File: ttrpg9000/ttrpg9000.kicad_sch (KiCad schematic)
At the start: 31 parts, among them SW1 SW_SPST, SW2 RotaryEncoder, SW3 RotaryEncoder, SW4 SW_Push, U1 LP2950-3.3_TO92, U2 ATtiny2313A-P

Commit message: Second pass of schematic, start layout
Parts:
- removed C1: 47u, symbol Device:C
- removed C14, C15, C9: 0.01u, symbol Device:C
- removed R7, R8: 10k, symbol Device:R
- removed SW2, SW3: RotaryEncoder, symbol Device:RotaryEncoder
- removed SW4: SW_Push, symbol Switch:SW_Push
- added C1: 47u, Capacitor_THT:CP_Radial_D5.0mm_P2.00mm, symbol Device:C_Polarized
- added C16, C4, C5, C7: 0.01u, Capacitor_THT:C_Axial_L5.1mm_D3.1mm_P7.50mm_Horizontal, symbol Device:C
- added R1, R2, R4: 10k, Resistor_THT:R_Axial_DIN0204_L3.6mm_D1.6mm_P5.08mm_Vertical, symbol Device:R
- added R12: 1M, Resistor_THT:R_Axial_DIN0204_L3.6mm_D1.6mm_P5.08mm_Vertical, symbol Device:R
- added R3, R9: 20k, Resistor_THT:R_Axial_DIN0204_L3.6mm_D1.6mm_P5.08mm_Vertical, symbol Device:R
- added SW2, SW3: RotaryEncoder_Switch, Project:PEC12R-4xxxF-Nxxxx, symbol Device:RotaryEncoder_Switch
- BT1: footprint (none) -> Project:BAT_BH800S
- C10, C11, C12, C13, C2, C3, C6: footprint (none) -> Capacitor_THT:C_Axial_L5.1mm_D3.1mm_P7.50mm_Horizontal
- C14: renamed from C4; footprint (none) -> Capacitor_THT:C_Axial_L5.1mm_D3.1mm_P7.50mm_Horizontal
- C15: renamed from C5; footprint (none) -> Capacitor_THT:C_Axial_L5.1mm_D3.1mm_P7.50mm_Horizontal
- C8: renamed from C7; footprint (none) -> Capacitor_THT:C_Axial_L5.1mm_D3.1mm_P7.50mm_Horizontal
- C9: renamed from C8; footprint (none) -> Capacitor_THT:C_Axial_L5.1mm_D3.1mm_P7.50mm_Horizontal
- DS1: footprint (none) -> Project:DOGM204
- R10: renamed from R3; footprint (none) -> Resistor_THT:R_Axial_DIN0204_L3.6mm_D1.6mm_P5.08mm_Vertical
- R11: renamed from R4; footprint (none) -> Resistor_THT:R_Axial_DIN0204_L3.6mm_D1.6mm_P5.08mm_Vertical
- R5: footprint (none) -> Resistor_THT:R_Axial_DIN0204_L3.6mm_D1.6mm_P5.08mm_Vertical
- R6: value 10k -> 1M; footprint (none) -> Resistor_THT:R_Axial_DIN0204_L3.6mm_D1.6mm_P5.08mm_Vertical
- R7: renamed from R1; footprint (none) -> Resistor_THT:R_Axial_DIN0204_L3.6mm_D1.6mm_P5.08mm_Vertical
- R8: renamed from R2; footprint (none) -> Resistor_THT:R_Axial_DIN0204_L3.6mm_D1.6mm_P5.08mm_Vertical
- SW1: footprint (none) -> Project:SW3x1_L101011ML04Q_CNK
- renumbered U2 to U1, U1 to U2
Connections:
- net +3V3: now also R10.1, R8.2, R2.2, R4.1, SW2.S2, SW3.S2
- net +6V: now also C1.1; no longer R10.1, R6.2, R8.2
- net GND: now also C15.1, R6.2, C1.2, C16.2, C4.2, C5.1, C7.2, R12.2, SW2.C, SW3.C; no longer C15.2
- net at R5.1: now also C5.2, R4.2, SW2.A; no longer U1.6 (PD2)
- net at R5.2: now also U1.8 (PD4); no longer R6.1
- net at C14.1, R7.2, R8.1: now also SW3.B
- net at R10.2, R11.1: now also C15.2, SW3.A; no longer C15.1
- net at R7.1: now also U1.6 (PD2); no longer U1.8 (PD4)
- net at U1.2 (PD0): now also C16.1, R12.1, R9.2
- net at U1.3 (PD1): now also R11.2
- net at U1.7 (PD3): now also R6.1, C7.1, R3.2; no longer R11.2
- net at U1.9 (PD5): now also R1.1
- new net: R9.1, SW3.S1
- new net: C4.1, R1.2, R2.1, SW2.B
- new net: R3.1, SW2.S1
- no-connect marks 5 -> 4
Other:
- moved on the sheet: C10, C11, C12, C13, C14, C15, C6, C8, C9, DS1, R10, R11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

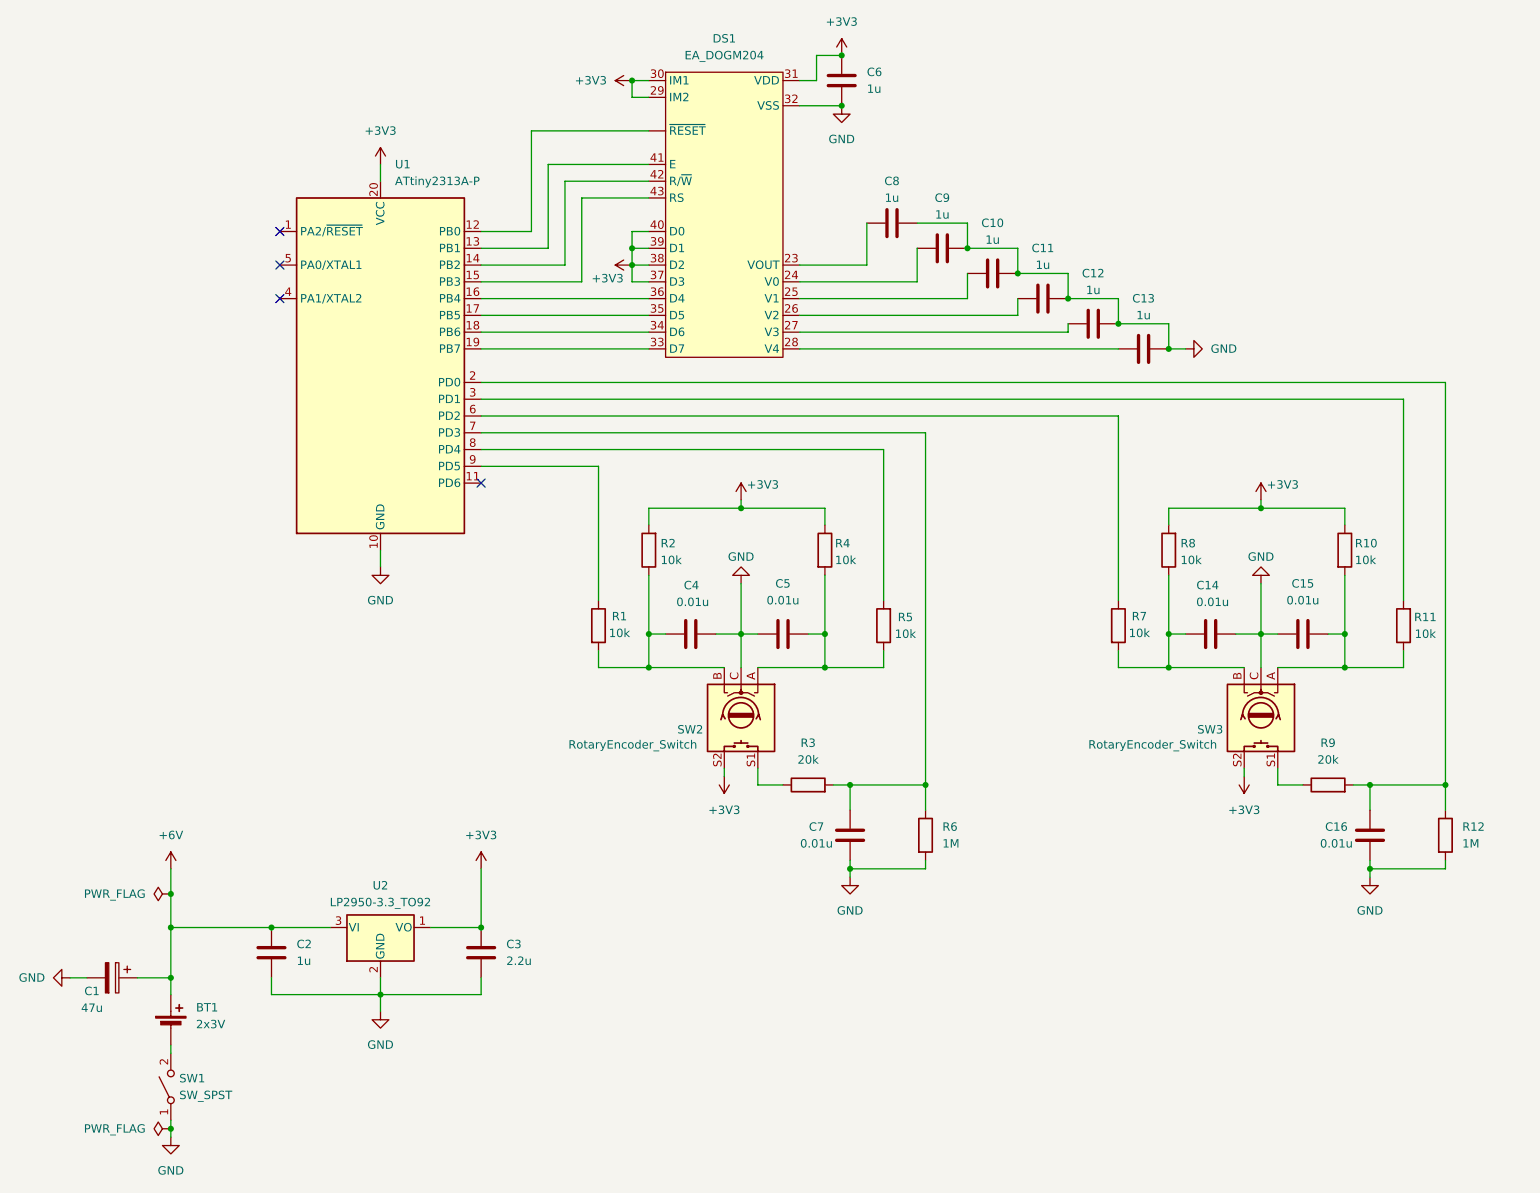
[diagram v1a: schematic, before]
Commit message: Clean up board layout
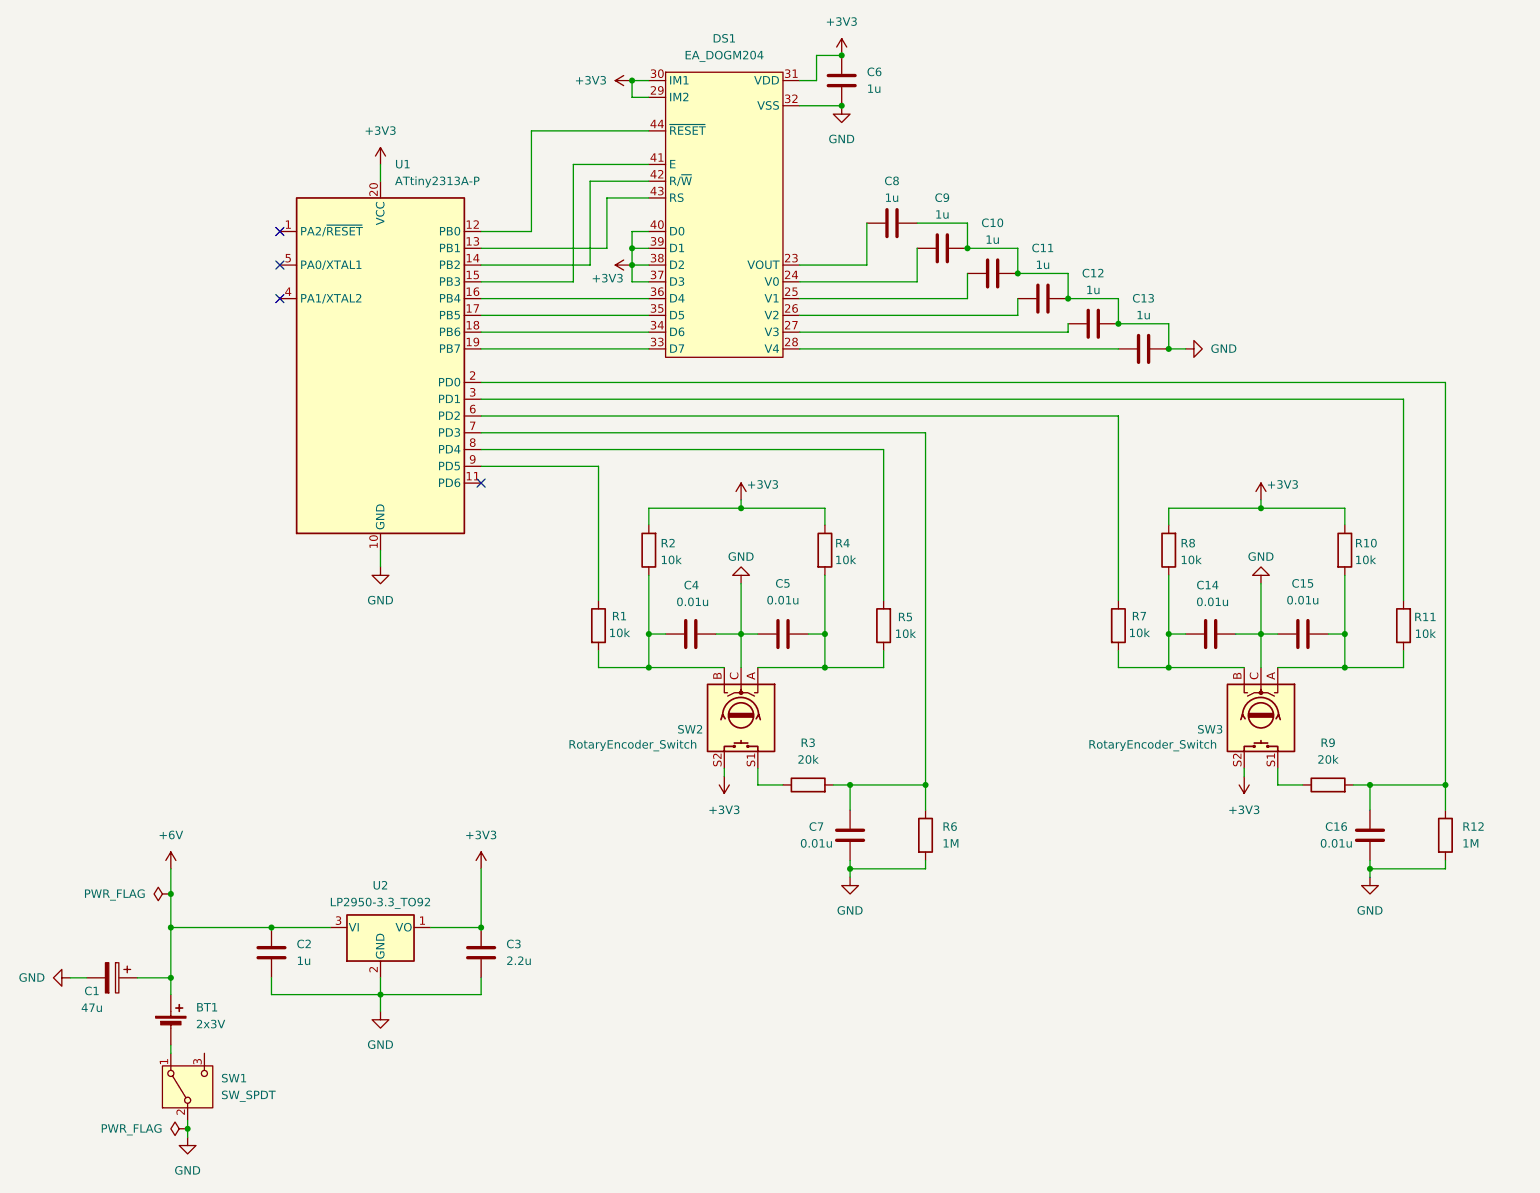
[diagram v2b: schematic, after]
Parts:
- removed SW1: SW_SPST, Project:SW3x1_L101011ML04Q_CNK, symbol Switch:SW_SPST
- added SW1: SW_SPDT, Project:OS102011MA1Q, symbol Switch:SW_SPDT
- R1, R10, R11, R12, R2, R3, R4, R5, R6, R7, R8, R9: footprint Resistor_THT:R_Axial_DIN0204_L3.6mm_D1.6mm_P5.08mm_Vertical -> Resistor_THT:R_Axial_DIN0204_L3.6mm_D1.6mm_P5.08mm_Horizontal
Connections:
- net GND: now also SW1.2 (B)
- net at U1.12 (PB0): now also DS1.44 (~{RESET}); no longer DS1. (~{RESET})
- net at DS1.41 (E): now also U1.15 (PB3); no longer U1.13 (PB1)
- net at DS1.43 (RS): now also U1.13 (PB1); no longer U1.15 (PB3)
- net at BT1.2 (-): now also SW1.1 (A)
